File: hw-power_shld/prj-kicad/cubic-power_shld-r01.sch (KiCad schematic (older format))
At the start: 17 parts

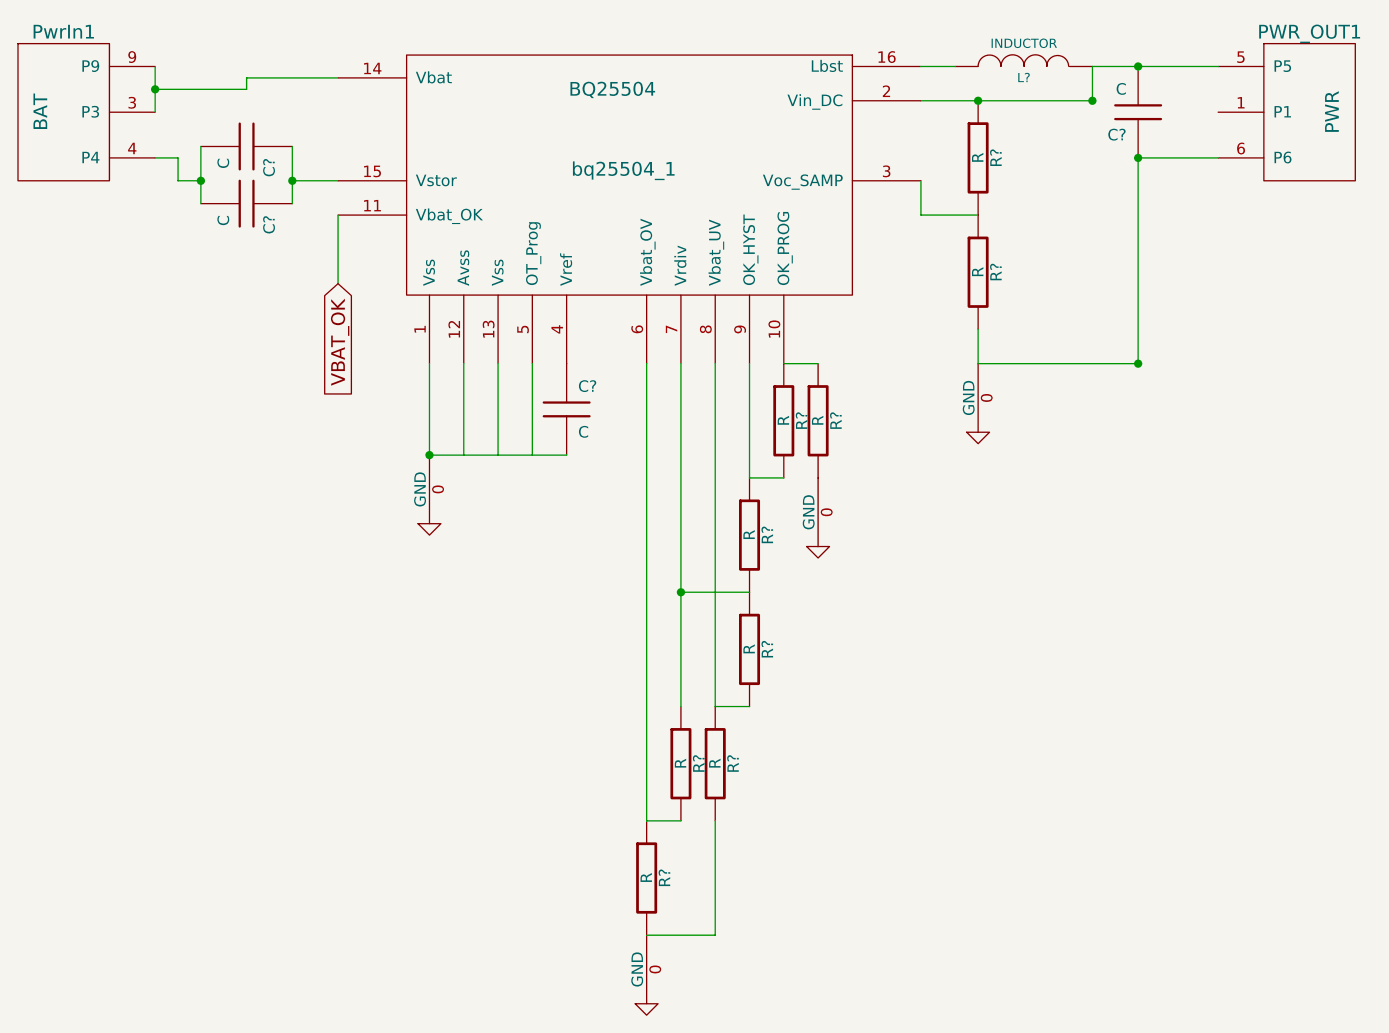
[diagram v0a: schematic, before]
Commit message: add footprint and label place netlist todo : brd
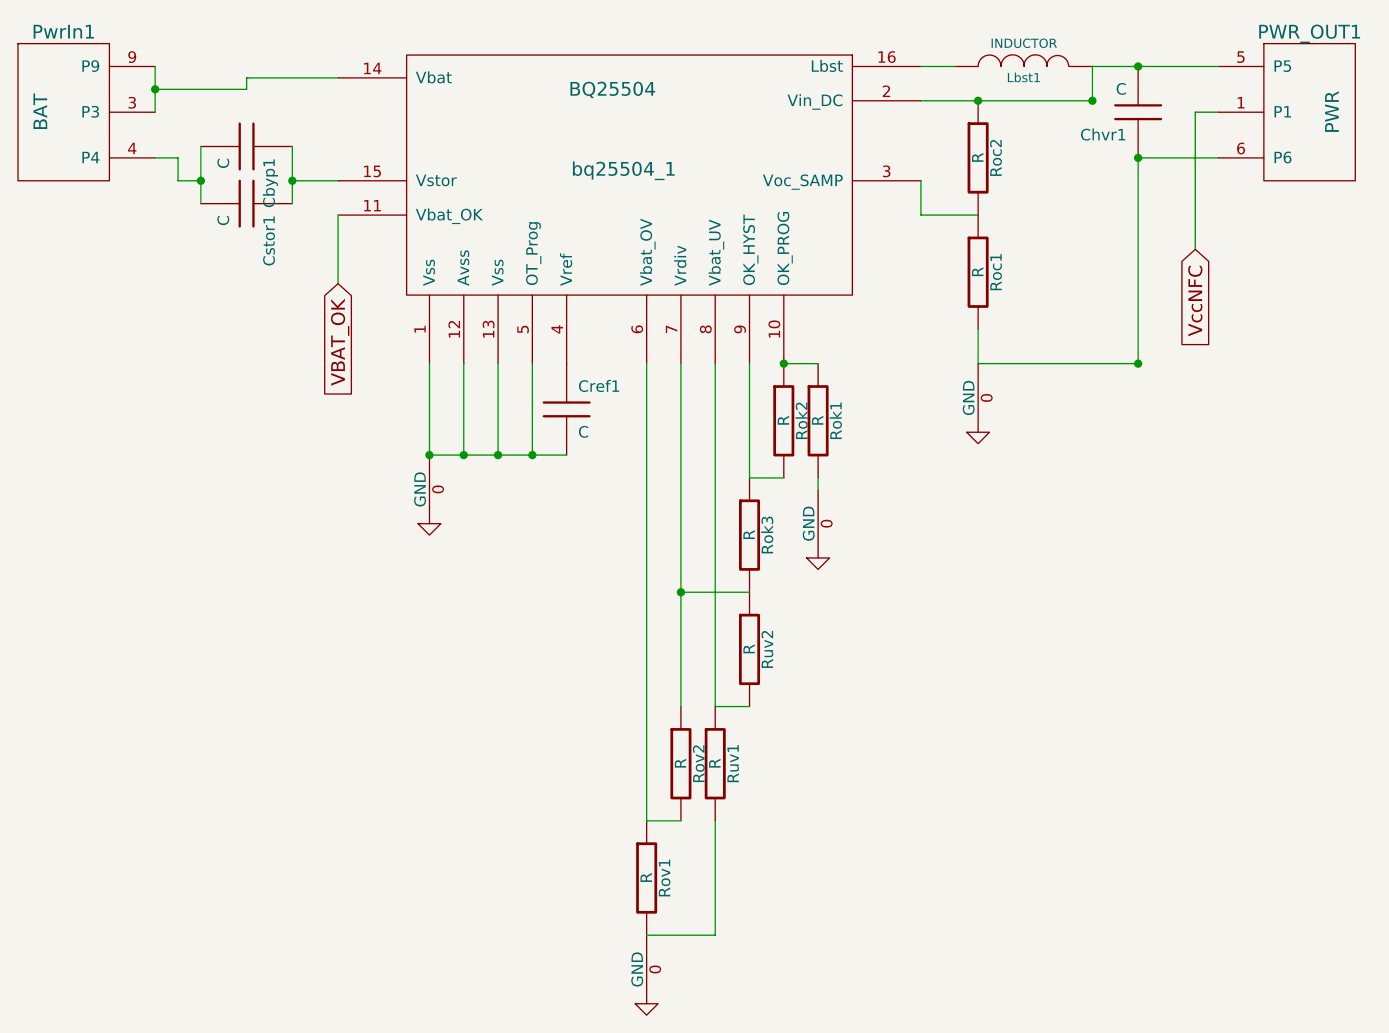
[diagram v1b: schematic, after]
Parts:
- gave numbers to parts that had none: 14
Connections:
- net labels added: VccNFC
- wire segments 43 -> 40
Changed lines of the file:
@@
 $EndComp
 $Comp
-L R R?
+L R Rov1
 U 1 1 55A38E03
 P 6050 6500
-F 0 "R?" V 6130 6500 50  0000 C CNN
+F 0 "Rov1" V 6130 6500 50  0000 C CNN
 F 1 "R" V 6050 6500 50  0000 C CNN
 F 2 "~" H 6050 6500 60  0000 C CNN
@@
 $EndComp
 $Comp
-L R R?
+L R Rov2
 U 1 1 55A38E16
 P 6200 6000
-F 0 "R?" V 6280 6000 50  0000 C CNN
+F 0 "Rov2" V 6280 6000 50  0000 C CNN
 F 1 "R" V 6200 6000 50  0000 C CNN
 F 2 "~" H 6200 6000 60  0000 C CNN
@@
 $EndComp
 $Comp
-L R R?
+L R Ruv1
 U 1 1 55A38E25
 P 6350 6000
-F 0 "R?" V 6430 6000 50  0000 C CNN
+F 0 "Ruv1" V 6430 6000 50  0000 C CNN
 F 1 "R" V 6350 6000 50  0000 C CNN
 F 2 "~" H 6350 6000 60  0000 C CNN
@@
 $EndComp
 $Comp
-L R R?
+L R Ruv2
 U 1 1 55A38E34
 P 6500 5500
-F 0 "R?" V 6580 5500 50  0000 C CNN
+F 0 "Ruv2" V 6580 5500 50  0000 C CNN
 F 1 "R" V 6500 5500 50  0000 C CNN
 F 2 "~" H 6500 5500 60  0000 C CNN
@@
 $EndComp
 $Comp
-L R R?
+L R Rok3
 U 1 1 55A38E43
 P 6500 5000
-F 0 "R?" V 6580 5000 50  0000 C CNN
+F 0 "Rok3" V 6580 5000 50  0000 C CNN
 F 1 "R" V 6500 5000 50  0000 C CNN
 F 2 "~" H 6500 5000 60  0000 C CNN
@@
 $EndComp
 $Comp
-L R R?
+L R Rok2
 U 1 1 55A38E52
 P 6650 4500
-F 0 "R?" V 6730 4500 50  0000 C CNN
+F 0 "Rok2" V 6730 4500 50  0000 C CNN
 F 1 "R" V 6650 4500 50  0000 C CNN
 F 2 "~" H 6650 4500 60  0000 C CNN
@@
 $EndComp
 $Comp
-L R R?
+L R Rok1
 U 1 1 55A38E61
 P 6800 4500
-F 0 "R?" V 6880 4500 50  0000 C CNN
+F 0 "Rok1" V 6880 4500 50  0000 C CNN
 F 1 "R" V 6800 4500 50  0000 C CNN
 F 2 "~" H 6800 4500 60  0000 C CNN
@@
 $EndComp
 $Comp
-L R R?
+L R Roc2
 U 1 1 55A38E70
 P 7500 3350
-F 0 "R?" V 7580 3350 50  0000 C CNN
+F 0 "Roc2" V 7580 3350 50  0000 C CNN
 F 1 "R" V 7500 3350 50  0000 C CNN
 F 2 "~" H 7500 3350 60  0000 C CNN
@@
 $EndComp
 $Comp
-L R R?
+L R Roc1
 U 1 1 55A38E7F
 P 7500 3850
-F 0 "R?" V 7580 3850 50  0000 C CNN
+F 0 "Roc1" V 7580 3850 50  0000 C CNN
 F 1 "R" V 7500 3850 50  0000 C CNN
 F 2 "~" H 7500 3850 60  0000 C CNN
@@
 $EndComp
 $Comp
-L GND #PWR?
+L GND #PWR01
 U 1 1 55A38FB0
 P 5100 4950
-F 0 "#PWR?" H 5100 4950 30  0001 C CNN
+F 0 "#PWR01" H 5100 4950 30  0001 C CNN
 F 1 "GND" H 5100 4880 30  0001 C CNN
 F 2 "~" H 5100 4950 60  0000 C CNN
@@
 $EndComp
 $Comp
-L C C?
+L C Cref1
 U 1 1 55A39774
 P 5700 4450
-F 0 "C?" H 5750 4550 50  0000 L CNN
+F 0 "Cref1" H 5750 4550 50  0000 L CNN
 F 1 "C" H 5750 4350 50  0000 L CNN
 F 2 "~" H 5700 4450 60  0000 C CNN
@@
 $EndComp
 $Comp
-L GND #PWR?
+L GND #PWR02
 U 1 1 55A3A2FD
 P 6050 7050
-F 0 "#PWR?" H 6050 7050 30  0001 C CNN
+F 0 "#PWR02" H 6050 7050 30  0001 C CNN
 F 1 "GND" H 6050 6980 30  0001 C CNN
 F 2 "~" H 6050 7050 60  0000 C CNN
@@
 $EndComp
 $Comp
-L GND #PWR?
+L GND #PWR03
 U 1 1 55A3A412
-P 6800 5050
-F 0 "#PWR?" H 6800 5050 30  0001 C CNN
-F 1 "GND" H 6800 4980 30  0001 C CNN
-F 2 "~" H 6800 5050 60  0000 C CNN
-F 3 "~" H 6800 5050 60  0000 C CNN
-	1    6800 5050
-	1    0    0    -1
-$EndComp
-$Comp
-L GND #PWR?
+P 6800 5100
+F 0 "#PWR03" H 6800 5100 30  0001 C CNN
+F 1 "GND" H 6800 5030 30  0001 C CNN
+F 2 "~" H 6800 5100 60  0000 C CNN
+F 3 "~" H 6800 5100 60  0000 C CNN
+	1    6800 5100
+	1    0    0    -1
+$EndComp
+$Comp
+L GND #PWR04
 U 1 1 55A3A5FF
 P 7500 4550
-F 0 "#PWR?" H 7500 4550 30  0001 C CNN
+F 0 "#PWR04" H 7500 4550 30  0001 C CNN
 F 1 "GND" H 7500 4480 30  0001 C CNN
 F 2 "~" H 7500 4550 60  0000 C CNN
@@
 $EndComp
 $Comp
-L INDUCTOR L?
+L INDUCTOR Lbst1
 U 1 1 55A3A9D0
 P 7700 2950
-F 0 "L?" V 7650 2950 40  0000 C CNN
+F 0 "Lbst1" V 7650 2950 40  0000 C CNN
 F 1 "INDUCTOR" V 7800 2950 40  0000 C CNN
 F 2 "~" H 7700 2950 60  0000 C CNN
@@
 $EndComp
 $Comp
-L C C?
+L C Cbyp1
 U 1 1 55A3AC29
 P 4300 3300
-F 0 "C?" H 4350 3400 50  0000 L CNN
+F 0 "Cbyp1" H 4350 3400 50  0000 L CNN
 F 1 "C" H 4350 3200 50  0000 L CNN
 F 2 "~" H 4300 3300 60  0000 C CNN
@@
 $EndComp
 $Comp
-L C C?
+L C Cstor1
 U 1 1 55A3AC45
 P 4300 3550
-F 0 "C?" H 4350 3650 50  0000 L CNN
+F 0 "Cstor1" H 4350 3650 50  0000 L CNN
 F 1 "C" H 4350 3450 50  0000 L CNN
 F 2 "~" H 4300 3550 60  0000 C CNN
@@
 VBAT_OK
 $Comp
-L C C?
+L C Chvr1
 U 1 1 55A3B330
 P 8200 3150
-F 0 "C?" H 8250 3250 50  0000 L CNN
+F 0 "Chvr1" H 8250 3250 50  0000 L CNN
 F 1 "C" H 8250 3050 50  0000 L CNN
 F 2 "~" H 8200 3150 60  0000 C CNN
@@
 Connection ~ 8000 3100
 Wire Wire Line
-	8000 2950 8200 2950
-Wire Wire Line
-	8200 2950 8550 2950
+	8000 2950 8550 2950
 Connection ~ 8200 3350
 Wire Wire Line
@@
 Connection ~ 7500 3100
 Wire Wire Line
-	7250 3100 7500 3100
-Wire Wire Line
-	7500 3100 8000 3100
+	7250 3100 8000 3100
 Wire Wire Line
 	7250 2950 7400 2950
@@
 	6500 5250 6200 5250
 Wire Wire Line
-	6200 4250 6200 5250
-Wire Wire Line
-	6200 5250 6200 5750
+	6200 4250 6200 5750
 Wire Wire Line
 	6350 5750 6500 5750
@@
 	5400 4650 5400 4250
 Wire Wire Line
-	5100 4650 5700 4650
-Wire Wire Line
 	5250 4250 5250 4650
 Wire Wire Line
 	5100 4250 5100 4650
 Wire Wire Line
-	3900 2950 3900 3050
-Wire Wire Line
-	3900 3050 3900 3150
+	3900 2950 3900 3150
 Wire Wire Line
 	3900 3050 4300 3050
@@
 Connection ~ 3900 3050
 Wire Wire Line
-	4500 3300 4500 3450
-Wire Wire Line
-	4500 3450 4500 3550
-Wire Wire Line
-	4100 3300 4100 3450
-Wire Wire Line
-	4100 3450 4100 3550
+	4500 3300 4500 3550
+Wire Wire Line
+	4100 3300 4100 3550
 Wire Wire Line
 	4500 3450 4700 3450
@@
 Wire Wire Line
 	8200 4250 7500 4250
+Wire Wire Line
+	8550 3150 8450 3150
+Wire Wire Line
+	8450 3150 8450 3750
+Text GLabel 8450 3750 3    60   Input ~ 0
+VccNFC
+Wire Wire Line
+	6800 4750 6800 4800
+Connection ~ 6650 4250
+Wire Wire Line
+	5100 4650 5700 4650
+Connection ~ 5250 4650
+Connection ~ 5400 4650
+Connection ~ 5550 4650
 $EndSCHEMATC

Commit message: correction erreur symbole masse placement des composants
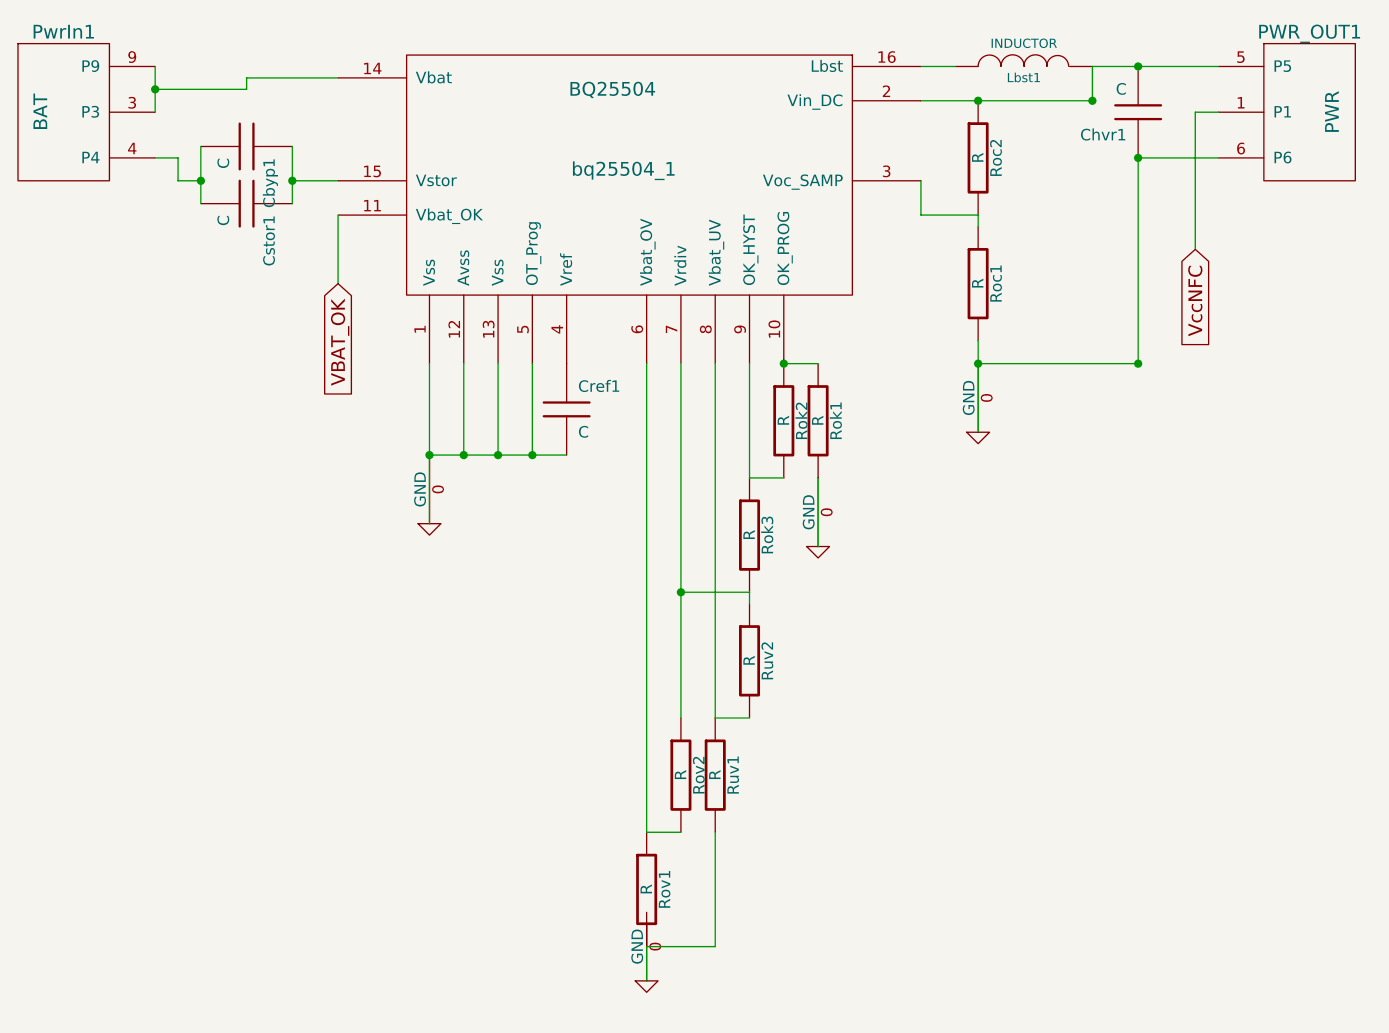
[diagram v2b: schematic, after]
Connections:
- net GND: now also Chvr1.1, Cref1.2, PWR_OUT1.6 (P6), Roc1.2, Rok1.2, Rov1.2, Ruv1.2, bq25504_1.1 (Vss), bq25504_1.12 (Avss), bq25504_1.13 (Vss), bq25504_1.5 (OT_Prog)
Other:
- moved on the sheet: Roc1, Rov1, Rov2, Ruv1, Ruv2
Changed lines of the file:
@@
 LIBS:r
 LIBS:inductor
-LIBS:cubic-power_shld-r01-cache
 EELAYER 27 0
 EELAYER END
@@
 Sheet 1 1
 Title "Cub'IC Power Shield"
-Date "13 jul 2015"
+Date "14 jul 2015"
 Rev "0.1"
 Comp "Agyga"
@@
 L R Rov1
 U 1 1 55A38E03
-P 6050 6500
-F 0 "Rov1" V 6130 6500 50  0000 C CNN
-F 1 "R" V 6050 6500 50  0000 C CNN
-F 2 "~" H 6050 6500 60  0000 C CNN
-F 3 "~" H 6050 6500 60  0000 C CNN
-	1    6050 6500
+P 6050 6550
+F 0 "Rov1" V 6130 6550 50  0000 C CNN
+F 1 "R" V 6050 6550 50  0000 C CNN
+F 2 "~" H 6050 6550 60  0000 C CNN
+F 3 "~" H 6050 6550 60  0000 C CNN
+	1    6050 6550
 	1    0    0    -1
 $EndComp
@@
 L R Rov2
 U 1 1 55A38E16
-P 6200 6000
-F 0 "Rov2" V 6280 6000 50  0000 C CNN
-F 1 "R" V 6200 6000 50  0000 C CNN
-F 2 "~" H 6200 6000 60  0000 C CNN
-F 3 "~" H 6200 6000 60  0000 C CNN
-	1    6200 6000
+P 6200 6050
+F 0 "Rov2" V 6280 6050 50  0000 C CNN
+F 1 "R" V 6200 6050 50  0000 C CNN
+F 2 "~" H 6200 6050 60  0000 C CNN
+F 3 "~" H 6200 6050 60  0000 C CNN
+	1    6200 6050
 	1    0    0    -1
 $EndComp
@@
 L R Ruv1
 U 1 1 55A38E25
-P 6350 6000
-F 0 "Ruv1" V 6430 6000 50  0000 C CNN
-F 1 "R" V 6350 6000 50  0000 C CNN
-F 2 "~" H 6350 6000 60  0000 C CNN
-F 3 "~" H 6350 6000 60  0000 C CNN
-	1    6350 6000
+P 6350 6050
+F 0 "Ruv1" V 6430 6050 50  0000 C CNN
+F 1 "R" V 6350 6050 50  0000 C CNN
+F 2 "~" H 6350 6050 60  0000 C CNN
+F 3 "~" H 6350 6050 60  0000 C CNN
+	1    6350 6050
 	1    0    0    -1
 $EndComp
@@
 L R Ruv2
 U 1 1 55A38E34
-P 6500 5500
-F 0 "Ruv2" V 6580 5500 50  0000 C CNN
-F 1 "R" V 6500 5500 50  0000 C CNN
-F 2 "~" H 6500 5500 60  0000 C CNN
-F 3 "~" H 6500 5500 60  0000 C CNN
-	1    6500 5500
+P 6500 5550
+F 0 "Ruv2" V 6580 5550 50  0000 C CNN
+F 1 "R" V 6500 5550 50  0000 C CNN
+F 2 "~" H 6500 5550 60  0000 C CNN
+F 3 "~" H 6500 5550 60  0000 C CNN
+	1    6500 5550
 	1    0    0    -1
 $EndComp
@@
 L R Roc1
 U 1 1 55A38E7F
-P 7500 3850
-F 0 "Roc1" V 7580 3850 50  0000 C CNN
-F 1 "R" V 7500 3850 50  0000 C CNN
-F 2 "~" H 7500 3850 60  0000 C CNN
-F 3 "~" H 7500 3850 60  0000 C CNN
-	1    7500 3850
+P 7500 3900
+F 0 "Roc1" V 7580 3900 50  0000 C CNN
+F 1 "R" V 7500 3900 50  0000 C CNN
+F 2 "~" H 7500 3900 60  0000 C CNN
+F 3 "~" H 7500 3900 60  0000 C CNN
+	1    7500 3900
 	1    0    0    -1
 $EndComp
@@
 L GND #PWR02
 U 1 1 55A3A2FD
-P 6050 7050
-F 0 "#PWR02" H 6050 7050 30  0001 C CNN
-F 1 "GND" H 6050 6980 30  0001 C CNN
-F 2 "~" H 6050 7050 60  0000 C CNN
-F 3 "~" H 6050 7050 60  0000 C CNN
-	1    6050 7050
+P 6050 6950
+F 0 "#PWR02" H 6050 6950 30  0001 C CNN
+F 1 "GND" H 6050 6880 30  0001 C CNN
+F 2 "~" H 6050 6950 60  0000 C CNN
+F 3 "~" H 6050 6950 60  0000 C CNN
+	1    6050 6950
 	1    0    0    -1
 $EndComp
@@
 L GND #PWR03
 U 1 1 55A3A412
-P 6800 5100
-F 0 "#PWR03" H 6800 5100 30  0001 C CNN
-F 1 "GND" H 6800 5030 30  0001 C CNN
-F 2 "~" H 6800 5100 60  0000 C CNN
-F 3 "~" H 6800 5100 60  0000 C CNN
-	1    6800 5100
+P 6800 5050
+F 0 "#PWR03" H 6800 5050 30  0001 C CNN
+F 1 "GND" H 6800 4980 30  0001 C CNN
+F 2 "~" H 6800 5050 60  0000 C CNN
+F 3 "~" H 6800 5050 60  0000 C CNN
+	1    6800 5050
 	1    0    0    -1
 $EndComp
@@
 	-1   0    0    1
 $EndComp
+Text GLabel 8450 3750 3    60   Input ~ 0
+VccNFC
 Wire Wire Line
 	8200 3350 8550 3350
@@
 	7250 2950 7400 2950
 Wire Wire Line
-	7500 4250 7500 4100
+	7500 4150 7500 4550
 Wire Wire Line
 	7250 3600 7500 3600
@@
 	7250 3450 7250 3600
 Wire Wire Line
-	6350 6750 6050 6750
-Wire Wire Line
-	6350 6250 6350 6750
-Wire Wire Line
-	6050 6250 6200 6250
+	6350 6300 6350 6800
+Wire Wire Line
+	6050 4250 6050 6300
 Connection ~ 6200 5250
 Wire Wire Line
 	6500 5250 6200 5250
 Wire Wire Line
-	6200 4250 6200 5750
-Wire Wire Line
-	6350 5750 6500 5750
-Wire Wire Line
-	6350 4250 6350 5750
+	6200 4250 6200 5800
+Wire Wire Line
+	6350 4250 6350 5800
 Wire Wire Line
 	6500 4250 6500 4750
@@
 Wire Wire Line
 	6650 4250 6800 4250
-Wire Wire Line
-	6050 4250 6050 6250
 Connection ~ 5100 4650
 Wire Wire Line
@@
 	5250 4250 5250 4650
 Wire Wire Line
-	5100 4250 5100 4650
+	5100 4250 5100 4950
 Wire Wire Line
 	3900 2950 3900 3150
@@
 Wire Wire Line
 	8450 3150 8450 3750
-Text GLabel 8450 3750 3    60   Input ~ 0
-VccNFC
-Wire Wire Line
-	6800 4750 6800 4800
 Connection ~ 6650 4250
 Wire Wire Line
@@
 Connection ~ 5400 4650
 Connection ~ 5550 4650
+Wire Wire Line
+	6800 4750 6800 5050
+Connection ~ 7500 4250
+Wire Wire Line
+	6050 6800 6050 6950
+Wire Wire Line
+	7500 3600 7500 3650
+Wire Wire Line
+	6050 6300 6200 6300
+Wire Wire Line
+	6350 5800 6500 5800
+Wire Wire Line
+	6500 5300 6500 5250
+Wire Wire Line
+	6350 6800 6050 6800
 $EndSCHEMATC
